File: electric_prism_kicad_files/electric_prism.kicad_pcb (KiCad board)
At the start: 2 copper layers, 52 x 35.5 mm, 33 parts, among them J1 Conn_02x03_Odd_Even, J2 USB_A, SW1 SW_Push, U1 ATmega328P-AU, U2 CH330N, Y1 Crystal

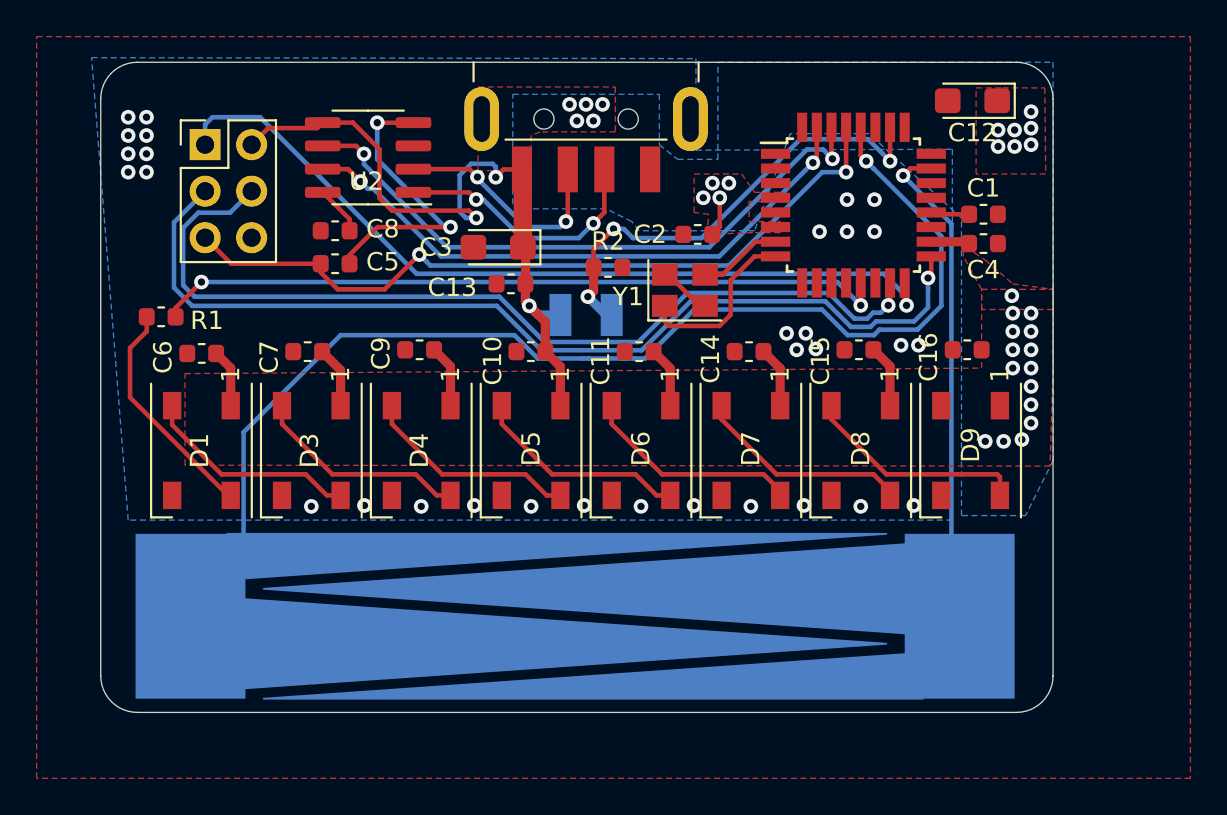
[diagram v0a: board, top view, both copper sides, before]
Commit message: Add files via upload
Updated design:
- Fixed asymmetry
- Added pull-up resistor to reset line
- Made curvy copper pours
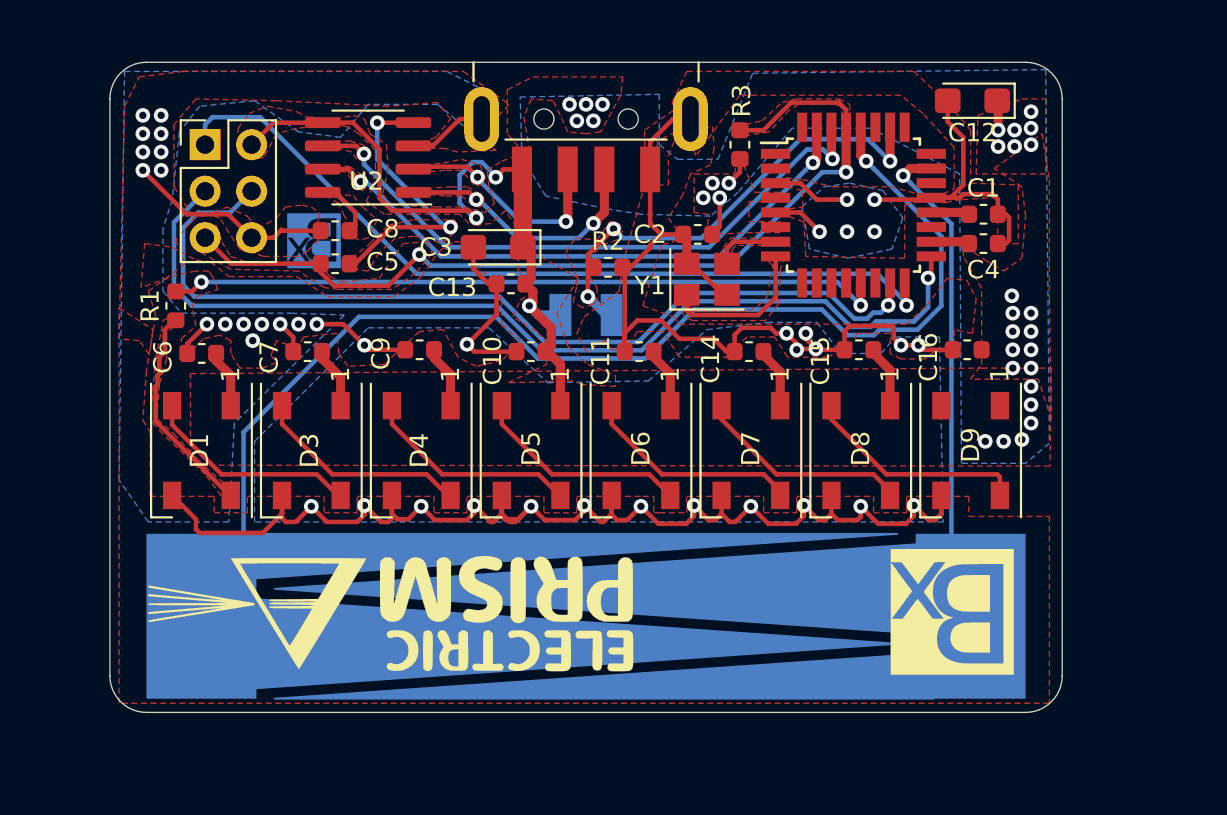
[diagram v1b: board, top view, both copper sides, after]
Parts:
- added G***: LOGO, bejcek:bx_logo_5500, B.Cu at (118.2, 91.8)
- added G***: LOGO, bejcek:bx_logo_2400, F.Cu at (153.0, 112.0)
- added G***: LOGO, bejcek:elec_prism_logo_smaller1000, F.Cu at (122.4, 112.2)
- added R3: 10k, Resistor_SMD:R_0603_1608Metric, F.Cu at (141.4, 86.5)
- SW1: value SW_Push -> CAP SLIDER
- moved Y1 1.34 mm to (139.6, 93.8)
- moved R1 1.00 mm to (110.6, 95.3), turned to 90 degrees
- moved SW1 0.60 mm to (153.0, 116.8)
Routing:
- net GND: track 2.90 -> 175.0 mm, vias 31 -> 41
- net RST: track 42.0 -> 49.4 mm
- net +5V: track 64.0 -> 67.5 mm
- net Net-(U1-Pad8): track 9.68 -> 8.45 mm
- net Net-(U1-Pad7): track 4.60 -> 3.64 mm
- net Net-(R1-Pad2): track 40.2 -> 39.4 mm
- net SLIDER_2: track 60.9 -> 61.8 mm
- net Net-(C8-Pad1): track 2.70 -> 3.36 mm
- net Net-(D1-Pad4): track 12.5 -> 11.9 mm
- added copper zone on F.Cu, net Net-(C5-Pad2)
- added copper zone on F.Cu, net Net-(C8-Pad1)
- added copper zone on F.Cu, net Net-(D1-Pad4)
- added copper zone on F.Cu, net Net-(D2-Pad1)
- added copper zone on F.Cu, net Net-(J2-Pad2)
- added copper zone on F.Cu, net Net-(J2-Pad3)
- added copper zone on F.Cu, net Net-(U1-Pad30)
- added copper zone on F.Cu, net Net-(U1-Pad31)
- added copper zone on F.Cu, net Net-(U1-Pad7)
- added copper zone on F.Cu, net Net-(U1-Pad8)
- added copper zone on F.Cu, net RST
